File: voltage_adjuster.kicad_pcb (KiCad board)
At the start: 2 copper layers, 16.2 x 15.2 mm, 24 parts, among them IC1 LDK130PU-R, IC2 MCP73832T-2ACI_MC, J1 UJC-H-G-SMT-1-P6-TR

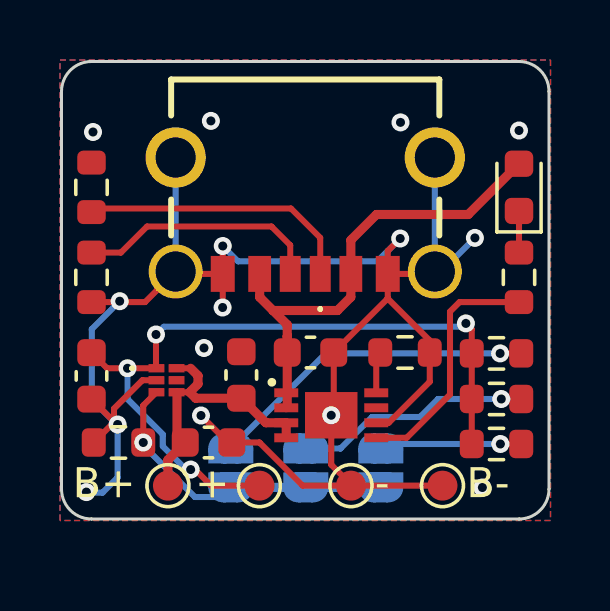
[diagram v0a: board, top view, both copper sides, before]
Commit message: move the usb-c a bit
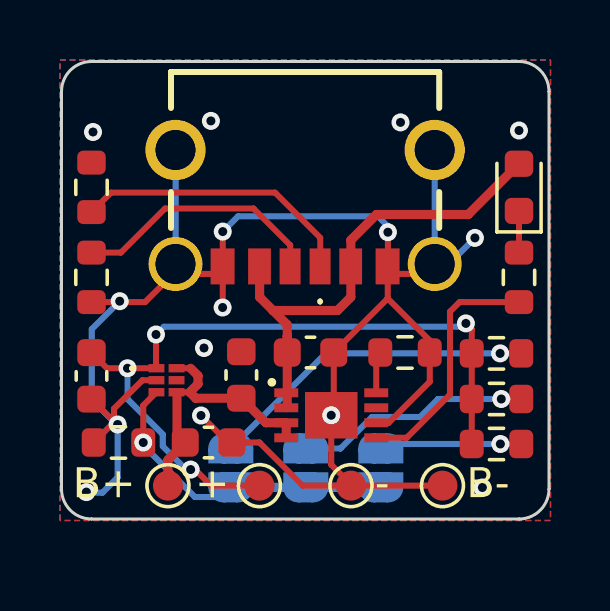
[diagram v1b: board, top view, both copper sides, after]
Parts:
- moved J1 0.25 mm to (64.1, 35.5)
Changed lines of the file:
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@@
 	(footprint "footprints_symbols:UJCHGSMT1P6TR"
 		(layer "F.Cu")
-		(at 64.125 35.75 180)
+		(at 64.12 35.5 180)
 		(descr "UJC-H-G-SMT-1-P6-TR-2")
 		(tags "Connector")
@@
 	)
 	(segment
-		(start 62.605 39.355)
-		(end 63.05 39.8)
+		(start 65.645 39.355)
+		(end 65.645 38.335)
 		(width 0.3048)
 		(layer "F.Cu")
@@
 	)
 	(segment
-		(start 63.05 39.8)
-		(end 65.2 39.8)
+		(start 65.2 39.8)
+		(end 65.645 39.355)
 		(width 0.3048)
 		(layer "F.Cu")
@@
 	)
 	(segment
-		(start 69.557499 36.6)
-		(end 71.25 34.907499)
+		(start 65.645 37.455)
+		(end 66.5 36.6)
 		(width 0.3048)
 		(layer "F.Cu")
@@
 	)
 	(segment
-		(start 65.645 39.355)
-		(end 65.645 38.58)
+		(start 65.64 38.33)
+		(end 65.645 38.325)
+		(width 0.3048)
+		(layer "F.Cu")
+		(net 1)
+	)
+	(segment
+		(start 65.645 38.335)
+		(end 65.64 38.33)
+		(width 0.3048)
+		(layer "F.Cu")
+		(net 1)
+	)
+	(segment
+		(start 62.605 38.335)
+		(end 62.605 39.355)
 		(width 0.3048)
 		(layer "F.Cu")
@@
 	)
 	(segment
-		(start 65.645 38.58)
+		(start 65.645 38.325)
 		(end 65.645 37.455)
 		(width 0.3048)
@@
 	)
 	(segment
-		(start 65.2 39.8)
-		(end 65.645 39.355)
+		(start 63.05 39.8)
+		(end 65.2 39.8)
 		(width 0.3048)
 		(layer "F.Cu")
@@
 	)
 	(segment
-		(start 65.645 37.455)
-		(end 66.5 36.6)
+		(start 63.525 40.65)
+		(end 63.525 43.008903)
 		(width 0.3048)
 		(layer "F.Cu")
@@
 	)
 	(segment
-		(start 63.525 40.65)
-		(end 63.525 43.008903)
+		(start 66.5 36.6)
+		(end 69.557499 36.6)
 		(width 0.3048)
 		(layer "F.Cu")
@@
 	)
 	(segment
-		(start 63.525 43.008903)
-		(end 63.49149 43.042413)
+		(start 62.6 38.33)
+		(end 62.605 38.335)
 		(width 0.3048)
 		(layer "F.Cu")
@@
 	)
 	(segment
-		(start 66.5 36.6)
-		(end 69.557499 36.6)
+		(start 69.557499 36.6)
+		(end 71.25 34.907499)
 		(width 0.3048)
 		(layer "F.Cu")
@@
 	)
 	(segment
-		(start 62.605 38.58)
-		(end 62.605 39.355)
+		(start 63.525 43.008903)
+		(end 63.49149 43.042413)
+		(width 0.3048)
+		(layer "F.Cu")
+		(net 1)
+	)
+	(segment
+		(start 62.605 39.355)
+		(end 63.05 39.8)
 		(width 0.3048)
 		(layer "F.Cu")
@@
 	)
 	(segment
-		(start 68.275 40.8)
-		(end 66.875 39.4)
+		(start 66.875 38.335)
+		(end 66.875 38.58)
 		(width 0.2032)
 		(layer "F.Cu")
@@
 	)
 	(segment
-		(start 66.875 37.815)
-		(end 67.29 37.4)
+		(start 68.275 40.8)
+		(end 66.875 39.4)
 		(width 0.2032)
 		(layer "F.Cu")
@@
 	)
 	(segment
+		(start 66.87 38.33)
+		(end 66.875 38.335)
+		(width 0.2032)
+		(layer "F.Cu")
+		(net 2)
+	)
+	(segment
 		(start 57.87 43.6)
 		(end 57.675 43.6)
@@
 	)
 	(segment
+		(start 61.375 38.325)
+		(end 61.375 37.17)
+		(width 0.2032)
+		(layer "F.Cu")
+		(net 2)
+	)
+	(segment
+		(start 61.37 38.33)
+		(end 61.375 38.325)
+		(width 0.2032)
+		(layer "F.Cu")
+		(net 2)
+	)
+	(segment
 		(start 61.675 44.2)
 		(end 62.6 44.2)
@@
 	)
 	(segment
-		(start 66.875 38.58)
-		(end 66.875 37.815)
-		(width 0.2032)
-		(layer "F.Cu")
-		(net 2)
-	)
-	(segment
 		(start 68.698758 45.638727)
 		(end 68.667485 45.67)
@@
 	)
 	(segment
+		(start 66.907587 43.542413)
+		(end 68.275 42.175)
+		(width 0.2032)
+		(layer "F.Cu")
+		(net 2)
+	)
+	(segment
 		(start 61.375 38.58)
-		(end 61.375 37.65)
+		(end 59.885 38.58)
 		(width 0.2032)
 		(layer "F.Cu")
@@
 	)
 	(segment
-		(start 66.907587 43.542413)
-		(end 68.275 42.175)
+		(start 66.88 38.32)
+		(end 66.87 38.33)
 		(width 0.2032)
 		(layer "F.Cu")
@@
 	)
 	(segment
-		(start 61.375 38.58)
-		(end 59.885 38.58)
+		(start 66.88 37.19)
+		(end 66.88 38.32)
 		(width 0.2032)
 		(layer "F.Cu")
@@
 	)
 	(via
-		(at 67.29 37.4)
+		(at 66.88 37.19)
 		(size 0.6)
 		(drill 0.3)
@@
 	)
 	(via
-		(at 61.375 37.65)
+		(at 61.375 37.17)
 		(size 0.6)
 		(drill 0.3)
@@
 	)
 	(segment
-		(start 61.885 38.16)
-		(end 61.375 37.65)
+		(start 59.8 38.25)
+		(end 59.805 38.245)
 		(width 0.2032)
 		(layer "B.Cu")
@@
 	)
 	(segment
-		(start 66.53 38.16)
-		(end 61.885 38.16)
+		(start 59.805 38.245)
+		(end 59.805 34.455)
 		(width 0.2032)
 		(layer "B.Cu")
@@
 	)
 	(segment
-		(start 68.445 38.5)
-		(end 68.445 34.7)
+		(start 66.88 37.19)
+		(end 66.88 36.99)
 		(width 0.2032)
 		(layer "B.Cu")
@@
 	)
 	(segment
-		(start 59.805 38.5)
-		(end 59.805 34.7)
+		(start 56.845606 45.87)
+		(end 56.828504 45.852898)
 		(width 0.2032)
 		(layer "B.Cu")
@@
 	)
 	(segment
-		(start 56.845606 45.87)
-		(end 56.828504 45.852898)
+		(start 59.805 34.455)
+		(end 59.8 34.45)
+		(width 0.2032)
+		(layer "B.Cu")
+		(net 2)
+	)
+	(segment
+		(start 66.55 36.66)
+		(end 61.885 36.66)
+		(width 0.2032)
+		(layer "B.Cu")
+		(net 2)
+	)
+	(segment
+		(start 68.44 34.695)
+		(end 68.445 34.7)
 		(width 0.2032)
 		(layer "B.Cu")
@@
 	)
 	(segment
+		(start 68.91 38.25)
+		(end 68.44 38.25)
+		(width 0.2032)
+		(layer "B.Cu")
+		(net 2)
+	)
+	(segment
+		(start 61.885 36.66)
+		(end 61.375 37.17)
+		(width 0.2032)
+		(layer "B.Cu")
+		(net 2)
+	)
+	(segment
 		(start 57.87 45.37)
 		(end 57.37 45.87)
@@
 	)
 	(segment
-		(start 68.445 38.5)
-		(end 68.66 38.5)
+		(start 66.88 36.99)
+		(end 66.55 36.66)
+		(width 0.2032)
+		(layer "B.Cu")
+		(net 2)
+	)
+	(segment
+		(start 68.44 38.25)
+		(end 68.44 34.45)
 		(width 0.2032)
 		(layer "B.Cu")
@@
 	)
 	(segment
-		(start 67.29 37.4)
-		(end 66.53 38.16)
+		(start 68.44 34.45)
+		(end 68.44 34.695)
 		(width 0.2032)
 		(layer "B.Cu")
@@
 	)
 	(segment
-		(start 68.66 38.5)
-		(end 69.78 37.38)
+		(start 69.78 37.38)
+		(end 68.91 38.25)
 		(width 0.2032)
 		(layer "B.Cu")
@@
 	)
 	(segment
+		(start 69.675 40.425)
+		(end 69.48 40.23)
+		(width 0.2032)
+		(layer "F.Cu")
+		(net 4)
+	)
+	(segment
 		(start 60.990229 45.638727)
 		(end 62.598758 45.638727)
@@
 	)
 	(segment
-		(start 69.675 40.425)
-		(end 69.48 40.23)
+		(start 69.675 41.23)
+		(end 69.675 40.425)
 		(width 0.2032)
 		(layer "F.Cu")
@@
 	)
 	(segment
-		(start 69.675 41.23)
-		(end 69.675 40.425)
-		(width 0.2032)
-		(layer "F.Cu")
-		(net 4)
-	)
-	(segment
 		(start 59.15 40.6)
 		(end 59.15 41.71)
@@
 	)
 	(segment
-		(start 58.85 37)
-		(end 63 37)
+		(start 63.625 38.325)
+		(end 63.62 38.33)
 		(width 0.2)
 		(layer "F.Cu")
@@
 	)
 	(segment
-		(start 57.98 37.87)
-		(end 58.85 37)
+		(start 59.45 36.4)
+		(end 62.4 36.4)
+		(width 0.2)
+		(layer "F.Cu")
+		(net 11)
+	)
+	(segment
+		(start 62.4 36.4)
+		(end 63.625 37.625)
 		(width 0.2)
 		(layer "F.Cu")
@@
 	)
 	(segment
-		(start 63 37)
-		(end 63.625 37.625)
+		(start 63.625 37.625)
+		(end 63.625 38.325)
 		(width 0.2)
 		(layer "F.Cu")
@@
 	)
 	(segment
-		(start 63.625 37.625)
-		(end 63.625 38.58)
+		(start 57.98 37.87)
+		(end 59.45 36.4)
 		(width 0.2)
 		(layer "F.Cu")
@@
 	)
 	(segment
-		(start 63.65 36.4)
-		(end 57.12 36.4)
+		(start 64.625 37.375)
+		(end 63.12 35.87)
+		(width 0.2)
+		(layer "F.Cu")
+		(net 12)
+	)
+	(segment
+		(start 63.12 35.87)
+		(end 57.65 35.87)
 		(width 0.2)
 		(layer "F.Cu")
@@
 	)
 	(segment
-		(start 57.12 36.4)
-		(end 57 36.52)
+		(start 64.625 38.325)
+		(end 64.625 37.375)
 		(width 0.2)
 		(layer "F.Cu")
@@
 	)
 	(segment
-		(start 64.625 37.375)
-		(end 63.65 36.4)
+		(start 57.65 35.87)
+		(end 57 36.52)
 		(width 0.2)
 		(layer "F.Cu")
@@
 	)
 	(segment
-		(start 64.625 38.58)
-		(end 64.625 37.375)
+		(start 64.62 38.33)
+		(end 64.625 38.325)
 		(width 0.2)
 		(layer "F.Cu")

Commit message: changed the size to be more uniform
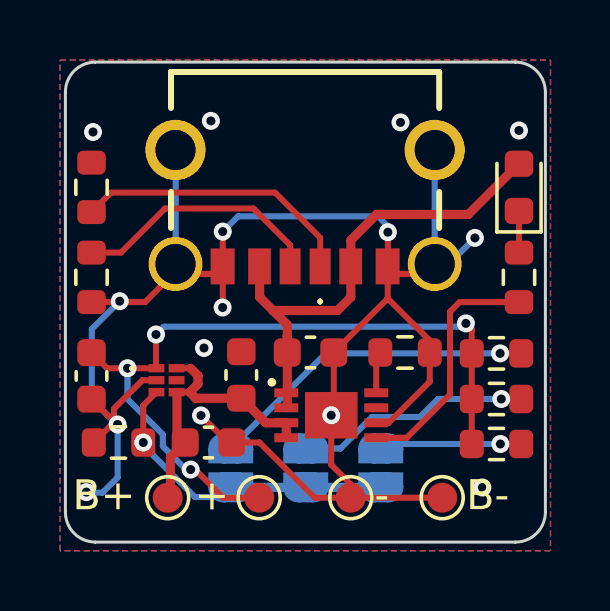
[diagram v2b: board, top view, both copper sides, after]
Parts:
- moved TP2 0.40 mm to (65.6, 46.0)
- moved TP4 0.40 mm to (59.5, 46.0)
- moved TP5 0.40 mm to (68.7, 46.0)
- moved TP1 0.40 mm to (62.6, 46.0)
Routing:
- net GND: track 61.3 -> 62.0 mm
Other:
- board size 16.2 x 15.2 mm -> 16 x 16 mm

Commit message: adjusted pcb size
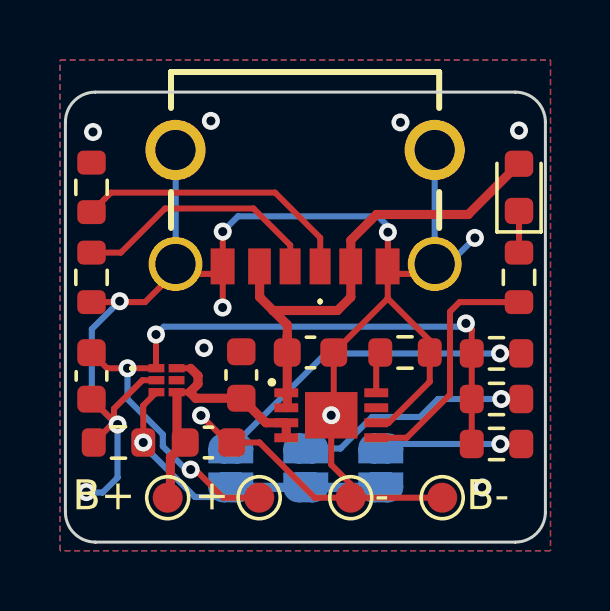
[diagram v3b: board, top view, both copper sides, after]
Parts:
- moved TP3 1.51 mm to (64.1, 36.5)
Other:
- board size 16 x 16 mm -> 16 x 15 mm
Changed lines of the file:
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@@
 	(footprint "Art:Salt-8x8"
 		(layer "B.Cu")
-		(at 64.1 34.95 180)
+		(at 64.08 36.46 180)
 		(property "Reference" "TP3"
 			(at 0 0 0)
@@
 	)
 	(gr_arc
-		(start 71.13 31.52)
-		(mid 71.837107 31.812893)
-		(end 72.13 32.52)
+		(start 71.13 32.52)
+		(mid 71.837107 32.812893)
+		(end 72.13 33.52)
 		(stroke
 			(width 0.1)
@@
 	)
 	(gr_arc
-		(start 56.13 32.52)
-		(mid 56.422893 31.812893)
-		(end 57.13 31.52)
+		(start 56.13 33.52)
+		(mid 56.422893 32.812893)
+		(end 57.13 32.52)
 		(stroke
 			(width 0.1)
@@
 	(gr_line
 		(start 56.13 46.52)
-		(end 56.13 32.52)
+		(end 56.13 33.52)
 		(stroke
 			(width 0.1)
-			(type default)
+			(type solid)
 		)
 		(layer "Edge.Cuts")
 	)
 	(gr_line
-		(start 57.13 31.52)
-		(end 71.13 31.52)
+		(start 57.13 32.52)
+		(end 71.13 32.52)
 		(stroke
 			(width 0.1)
@@
 	)
 	(gr_line
-		(start 72.13 32.52)
+		(start 72.13 33.52)
 		(end 72.13 46.52)
 		(stroke
 			(width 0.1)
-			(type default)
+			(type solid)
 		)
 		(layer "Edge.Cuts")
